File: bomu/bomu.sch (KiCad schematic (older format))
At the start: 29 parts, among them U1 NRF52840-CKAA-R7

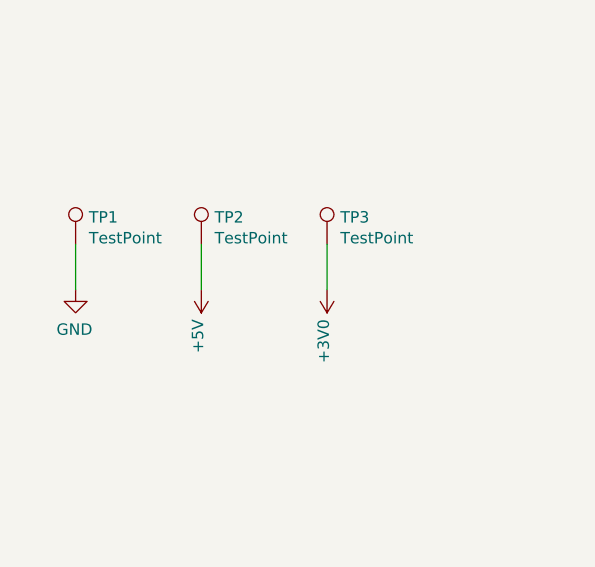
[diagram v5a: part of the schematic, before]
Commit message: Updating footprints. Adding SWD pads
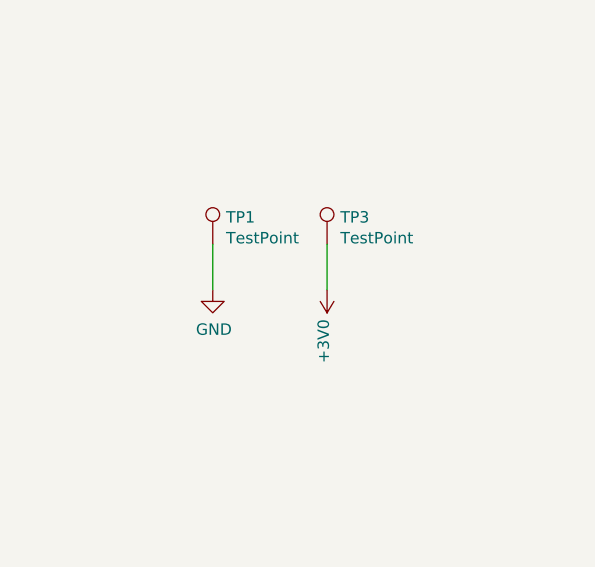
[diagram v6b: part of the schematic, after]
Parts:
- removed TP2: TestPoint, TestPoint:TestPoint_Pad_D1.0mm, symbol Connector:TestPoint
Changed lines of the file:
@@
 Using datasheet figure 216: Circuit configuration no. 1 schematic for CKAA WLCSP
-$Comp
-L Connector:TestPoint TP1
-U 1 1 5FCE36DE
-P 750 4500
-F 0 "TP1" H 808 4618 50  0000 L CNN
-F 1 "TestPoint" H 808 4527 50  0000 L CNN
-F 2 "TestPoint:TestPoint_Pad_D1.0mm" H 950 4500 50  0001 C CNN
-F 3 "~" H 950 4500 50  0001 C CNN
-	1    750  4500
-	1    0    0    -1
-$EndComp
-$Comp
-L Connector:TestPoint TP2
-U 1 1 5FCE40CD
-P 1300 4500
-F 0 "TP2" H 1358 4618 50  0000 L CNN
-F 1 "TestPoint" H 1358 4527 50  0000 L CNN
-F 2 "TestPoint:TestPoint_Pad_D1.0mm" H 1500 4500 50  0001 C CNN
-F 3 "~" H 1500 4500 50  0001 C CNN
-	1    1300 4500
-	1    0    0    -1
-$EndComp
-$Comp
-L Connector:TestPoint TP3
-U 1 1 5FCE4A4F
-P 1850 4500
-F 0 "TP3" H 1908 4618 50  0000 L CNN
-F 1 "TestPoint" H 1908 4527 50  0000 L CNN
-F 2 "TestPoint:TestPoint_Pad_D1.0mm" H 2050 4500 50  0001 C CNN
-F 3 "~" H 2050 4500 50  0001 C CNN
-	1    1850 4500
-	1    0    0    -1
-$EndComp
 $Comp
 L Connector:TestPoint TP4
@@
 	1    0    0    -1
 $EndComp
-$Comp
-L power:GND #PWR0124
-U 1 1 5FCFFB30
-P 750 4700
-F 0 "#PWR0124" H 750 4450 50  0001 C CNN
-F 1 "GND" H 755 4527 50  0000 C CNN
-F 2 "" H 750 4700 50  0001 C CNN
-F 3 "" H 750 4700 50  0001 C CNN
-	1    750  4700
-	-1   0    0    -1
-$EndComp
-Wire Wire Line
-	750  4500 750  4700
-$Comp
-L power:+5V #PWR0125
-U 1 1 5FD03B63
-P 1300 4700
-F 0 "#PWR0125" H 1300 4550 50  0001 C CNN
-F 1 "+5V" V 1315 4828 50  0000 L CNN
-F 2 "" H 1300 4700 50  0001 C CNN
-F 3 "" H 1300 4700 50  0001 C CNN
-	1    1300 4700
-	-1   0    0    1
-$EndComp
-Wire Wire Line
-	1300 4500 1300 4700
 $Comp
 L power:+3V0 #PWR0126
@@
 	-1   0    0    -1
 $EndComp
+$Comp
+L Connector:TestPoint TP3
+U 1 1 5FCE4A4F
+P 1850 4500
+F 0 "TP3" H 1908 4618 50  0000 L CNN
+F 1 "TestPoint" H 1908 4527 50  0000 L CNN
+F 2 "TestPoint:TestPoint_Pad_D1.0mm" H 2050 4500 50  0001 C CNN
+F 3 "~" H 2050 4500 50  0001 C CNN
+	1    1850 4500
+	1    0    0    -1
+$EndComp
+$Comp
+L Connector:TestPoint TP1
+U 1 1 5FDB96C2
+P 1350 4500
+F 0 "TP1" H 1408 4618 50  0000 L CNN
+F 1 "TestPoint" H 1408 4527 50  0000 L CNN
+F 2 "TestPoint:TestPoint_Pad_D1.0mm" H 1550 4500 50  0001 C CNN
+F 3 "~" H 1550 4500 50  0001 C CNN
+	1    1350 4500
+	1    0    0    -1
+$EndComp
+$Comp
+L power:GND #PWR?
+U 1 1 5FDBCBF5
+P 1350 4700
+F 0 "#PWR?" H 1350 4450 50  0001 C CNN
+F 1 "GND" H 1355 4527 50  0000 C CNN
+F 2 "" H 1350 4700 50  0001 C CNN
+F 3 "" H 1350 4700 50  0001 C CNN
+	1    1350 4700
+	1    0    0    -1
+$EndComp
+Wire Wire Line
+	1350 4700 1350 4500
 $EndSCHEMATC

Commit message: Current work on ground planes
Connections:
- net XTAL_P: now reaches C4.2, U1.A1 (XC1), XTAL1.1
- net XTAL_N: now reaches C5.1, U1.A2 (XC2), XTAL1.3
- net XL1 renamed 32XTAL_P
- net XL2 renamed 32XTAL_N
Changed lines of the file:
@@
 $EndComp
 $Comp
-L power:GND #PWR?
+L power:GND #PWR0124
 U 1 1 5FDBCBF5
 P 1350 4700
-F 0 "#PWR?" H 1350 4450 50  0001 C CNN
+F 0 "#PWR0124" H 1350 4450 50  0001 C CNN
 F 1 "GND" H 1355 4527 50  0000 C CNN
 F 2 "" H 1350 4700 50  0001 C CNN
@@
 Wire Wire Line
 	1350 4700 1350 4500
+Text Label 6050 950  0    50   ~ 0
+XTAL_P
+Text Label 6050 1950 0    50   ~ 0
+XTAL_N
+Text Label 4550 2800 0    50   ~ 0
+32XTAL_P
+Text Label 4550 2900 0    50   ~ 0
+32XTAL_N
 $EndSCHEMATC

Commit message: Current progress on BOMU 1.0.0
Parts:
- added C_RF1, C_RF2: DNP, Capacitor_SMD:C_0201_0603Metric, symbol Device:C_Small
- added L3: DNP, Inductor_SMD:L_0201_0603Metric, symbol Device:L
- added TP10, TP7, TP8, TP9: TestPoint, TestPoint:TestPoint_Pad_D1.0mm, symbol Connector:TestPoint
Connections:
- net +3V0: now also TP7.1
- net GND: now also C_RF1.2, C_RF2.2, TP8.1
- net at ANT1.FEED: now also C_RF2.1, L3.1; no longer L2.1
- net P0.04: now reaches U1.C10 (P0.04/AIN2)
- net P0.04: now also TP9.1
- net P0.05: now reaches U1.D10 (P0.05/AIN3)
- net P0.05: now also TP10.1
- net USB_N: now reaches U1.J8 (D-), USB1.2 (DP)
- net USB_P: now reaches U1.K8 (D+), USB1.3 (DM)
- new net: C_RF1.1, L2.1, L3.2
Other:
- moved on the sheet: ANT1, TP3
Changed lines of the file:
@@
 L W3008:W3008 ANT1
 U 1 1 5FCE2E26
-P 9750 2350
-F 0 "ANT1" H 9623 2438 50  0000 R CNN
-F 1 "W3008" H 9623 2347 50  0000 R CNN
-F 2 "W3008:ANTENNA_W3008" H 9750 2350 50  0001 L BNN
-F 3 "" H 9750 2350 50  0001 L BNN
-F 4 "Manufacturer recommendations" H 9750 2350 50  0001 L BNN "STANDARD"
-F 5 "PulseLarsen Antennas" H 9750 2350 50  0001 L BNN "MANUFACTURER"
-	1    9750 2350
+P 10450 2350
+F 0 "ANT1" H 10323 2438 50  0000 R CNN
+F 1 "W3008" H 10323 2347 50  0000 R CNN
+F 2 "W3008:ANTENNA_W3008" H 10450 2350 50  0001 L BNN
+F 3 "" H 10450 2350 50  0001 L BNN
+F 4 "Manufacturer recommendations" H 10450 2350 50  0001 L BNN "STANDARD"
+F 5 "PulseLarsen Antennas" H 10450 2350 50  0001 L BNN "MANUFACTURER"
+	1    10450 2350
 	1    0    0    -1
 $EndComp
@@
 L power:GND #PWR0103
 U 1 1 5FCE84AA
-P 9950 3200
-F 0 "#PWR0103" H 9950 2950 50  0001 C CNN
-F 1 "GND" H 9955 3027 50  0000 C CNN
-F 2 "" H 9950 3200 50  0001 C CNN
-F 3 "" H 9950 3200 50  0001 C CNN
-	1    9950 3200
-	-1   0    0    -1
-$EndComp
-Wire Wire Line
-	9750 2450 9750 2800
-Wire Wire Line
-	9950 2450 9950 3200
+P 10650 3200
+F 0 "#PWR0103" H 10650 2950 50  0001 C CNN
+F 1 "GND" H 10655 3027 50  0000 C CNN
+F 2 "" H 10650 3200 50  0001 C CNN
+F 3 "" H 10650 3200 50  0001 C CNN
+	1    10650 3200
+	-1   0    0    -1
+$EndComp
+Wire Wire Line
+	10450 2450 10450 2800
+Wire Wire Line
+	10650 2450 10650 3200
 $Comp
 L ABS06-107-32.768KHZ-T:ABS06-107-32.768KHZ-T XTAL2
@@
 Connection ~ 8950 2800
 Wire Wire Line
-	9750 2800 9350 2800
-Wire Wire Line
 	7300 2800 8400 2800
 Wire Wire Line
@@
 L power:+3V0 #PWR0126
 U 1 1 5FD06B8A
-P 1850 4700
-F 0 "#PWR0126" H 1850 4550 50  0001 C CNN
-F 1 "+3V0" V 1865 4828 50  0000 L CNN
-F 2 "" H 1850 4700 50  0001 C CNN
-F 3 "" H 1850 4700 50  0001 C CNN
-	1    1850 4700
+P 2000 4700
+F 0 "#PWR0126" H 2000 4550 50  0001 C CNN
+F 1 "+3V0" V 2015 4828 50  0000 L CNN
+F 2 "" H 2000 4700 50  0001 C CNN
+F 3 "" H 2000 4700 50  0001 C CNN
+	1    2000 4700
 	-1   0    0    1
 $EndComp
 Wire Wire Line
-	1850 4500 1850 4700
+	2000 4500 2000 4700
 Wire Wire Line
 	3500 4600 3500 4500
@@
 L Connector:TestPoint TP3
 U 1 1 5FCE4A4F
-P 1850 4500
-F 0 "TP3" H 1908 4618 50  0000 L CNN
-F 1 "TestPoint" H 1908 4527 50  0000 L CNN
-F 2 "TestPoint:TestPoint_Pad_D1.0mm" H 2050 4500 50  0001 C CNN
-F 3 "~" H 2050 4500 50  0001 C CNN
-	1    1850 4500
+P 2000 4500
+F 0 "TP3" H 2058 4618 50  0000 L CNN
+F 1 "TestPoint" H 2058 4527 50  0000 L CNN
+F 2 "TestPoint:TestPoint_Pad_D1.0mm" H 2200 4500 50  0001 C CNN
+F 3 "~" H 2200 4500 50  0001 C CNN
+	1    2000 4500
 	1    0    0    -1
 $EndComp
@@
 Text Label 4550 2900 0    50   ~ 0
 32XTAL_N
+Text Label 8400 3000 0    50   ~ 0
+USB_N
+Text Label 8100 3100 0    50   ~ 0
+USB_P
+$Comp
+L Connector:TestPoint TP7
+U 1 1 5FE65C61
+P 2700 4500
+F 0 "TP7" H 2758 4618 50  0000 L CNN
+F 1 "TestPoint" H 2758 4527 50  0000 L CNN
+F 2 "TestPoint:TestPoint_Pad_D1.0mm" H 2900 4500 50  0001 C CNN
+F 3 "~" H 2900 4500 50  0001 C CNN
+	1    2700 4500
+	1    0    0    -1
+$EndComp
+$Comp
+L power:+3V0 #PWR0125
+U 1 1 5FE66259
+P 2700 4700
+F 0 "#PWR0125" H 2700 4550 50  0001 C CNN
+F 1 "+3V0" V 2715 4828 50  0000 L CNN
+F 2 "" H 2700 4700 50  0001 C CNN
+F 3 "" H 2700 4700 50  0001 C CNN
+	1    2700 4700
+	-1   0    0    1
+$EndComp
+Wire Wire Line
+	2700 4500 2700 4700
+$Comp
+L Connector:TestPoint TP8
+U 1 1 5FE69185
+P 900 4500
+F 0 "TP8" H 958 4618 50  0000 L CNN
+F 1 "TestPoint" H 958 4527 50  0000 L CNN
+F 2 "TestPoint:TestPoint_Pad_D1.0mm" H 1100 4500 50  0001 C CNN
+F 3 "~" H 1100 4500 50  0001 C CNN
+	1    900  4500
+	1    0    0    -1
+$EndComp
+$Comp
+L power:GND #PWR0127
+U 1 1 5FE69C17
+P 900 4700
+F 0 "#PWR0127" H 900 4450 50  0001 C CNN
+F 1 "GND" H 905 4527 50  0000 C CNN
+F 2 "" H 900 4700 50  0001 C CNN
+F 3 "" H 900 4700 50  0001 C CNN
+	1    900  4700
+	1    0    0    -1
+$EndComp
+Wire Wire Line
+	900  4500 900  4700
+$Comp
+L Device:L L3
+U 1 1 5FEBFB1D
+P 9750 2800
+F 0 "L3" V 9940 2800 50  0000 C CNN
+F 1 "DNP" V 9849 2800 50  0000 C CNN
+F 2 "Inductor_SMD:L_0201_0603Metric" H 9750 2800 50  0001 C CNN
+F 3 "~" H 9750 2800 50  0001 C CNN
+	1    9750 2800
+	0    1    -1   0
+$EndComp
+$Comp
+L Device:C_Small C_RF1
+U 1 1 5FEC0D2F
+P 9550 3000
+F 0 "C_RF1" H 9642 3046 50  0000 L CNN
+F 1 "DNP" H 9642 2955 50  0000 L CNN
+F 2 "Capacitor_SMD:C_0201_0603Metric" H 9550 3000 50  0001 C CNN
+F 3 "~" H 9550 3000 50  0001 C CNN
+	1    9550 3000
+	-1   0    0    -1
+$EndComp
+$Comp
+L Device:C_Small C_RF2
+U 1 1 5FEC1A7E
+P 9950 3000
+F 0 "C_RF2" H 10042 3046 50  0000 L CNN
+F 1 "DNP" H 10042 2955 50  0000 L CNN
+F 2 "Capacitor_SMD:C_0201_0603Metric" H 9950 3000 50  0001 C CNN
+F 3 "~" H 9950 3000 50  0001 C CNN
+	1    9950 3000
+	-1   0    0    -1
+$EndComp
+Wire Wire Line
+	9350 2800 9550 2800
+Wire Wire Line
+	9900 2800 9950 2800
+Wire Wire Line
+	9550 2900 9550 2800
+Connection ~ 9550 2800
+Wire Wire Line
+	9550 2800 9600 2800
+Wire Wire Line
+	9950 2900 9950 2800
+Connection ~ 9950 2800
+Wire Wire Line
+	9950 2800 10450 2800
+$Comp
+L power:GND #PWR0128
+U 1 1 5FECD87E
+P 9550 3200
+F 0 "#PWR0128" H 9550 2950 50  0001 C CNN
+F 1 "GND" H 9555 3027 50  0000 C CNN
+F 2 "" H 9550 3200 50  0001 C CNN
+F 3 "" H 9550 3200 50  0001 C CNN
+	1    9550 3200
+	-1   0    0    -1
+$EndComp
+$Comp
+L power:GND #PWR0129
+U 1 1 5FECDCAD
+P 9950 3200
+F 0 "#PWR0129" H 9950 2950 50  0001 C CNN
+F 1 "GND" H 9955 3027 50  0000 C CNN
+F 2 "" H 9950 3200 50  0001 C CNN
+F 3 "" H 9950 3200 50  0001 C CNN
+	1    9950 3200
+	-1   0    0    -1
+$EndComp
+Wire Wire Line
+	9550 3100 9550 3200
+Wire Wire Line
+	9950 3100 9950 3200
+$Comp
+L Connector:TestPoint TP9
+U 1 1 5FF4F095
+P 4450 3450
+F 0 "TP9" H 4508 3568 50  0000 L CNN
+F 1 "TestPoint" H 4508 3477 50  0000 L CNN
+F 2 "TestPoint:TestPoint_Pad_D1.0mm" H 4650 3450 50  0001 C CNN
+F 3 "~" H 4650 3450 50  0001 C CNN
+	1    4450 3450
+	0    -1   -1   0
+$EndComp
+$Comp
+L Connector:TestPoint TP10
+U 1 1 5FF4F50B
+P 4150 3600
+F 0 "TP10" H 4208 3718 50  0000 L CNN
+F 1 "TestPoint" H 4208 3627 50  0000 L CNN
+F 2 "TestPoint:TestPoint_Pad_D1.0mm" H 4350 3600 50  0001 C CNN
+F 3 "~" H 4350 3600 50  0001 C CNN
+	1    4150 3600
+	0    -1   -1   0
+$EndComp
+Wire Wire Line
+	5100 3200 4550 3200
+Wire Wire Line
+	4550 3200 4550 3450
+Wire Wire Line
+	4550 3450 4450 3450
+Wire Wire Line
+	5100 3300 4650 3300
+Wire Wire Line
+	4650 3300 4650 3600
+Wire Wire Line
+	4650 3600 4150 3600
+Text Label 4550 3200 0    50   ~ 0
+P0.04
+Text Label 4650 3300 0    50   ~ 0
+P0.05
 $EndSCHEMATC
